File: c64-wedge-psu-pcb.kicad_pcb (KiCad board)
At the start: 2 copper layers, 70 x 54 mm, 22 parts, among them U1 LM2576T-ADJ

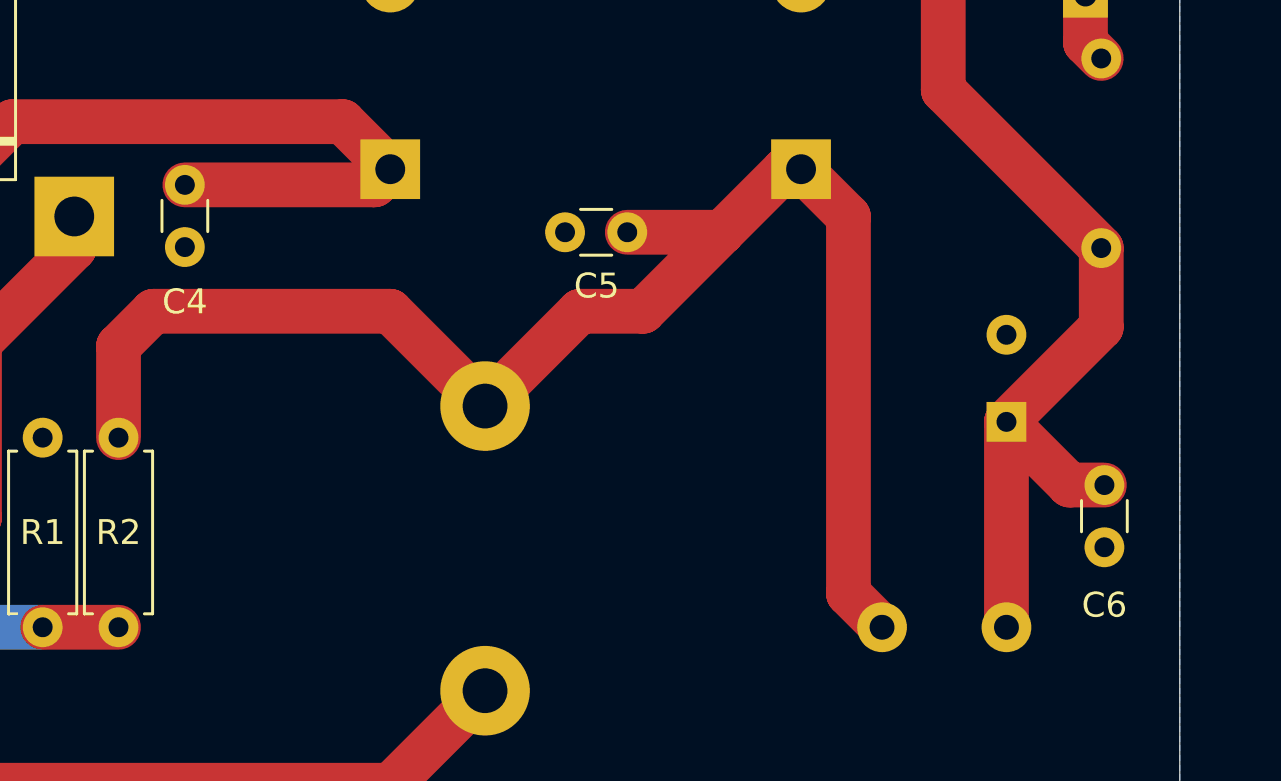
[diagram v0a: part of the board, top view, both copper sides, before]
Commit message: update ceramics with part number and update footprints
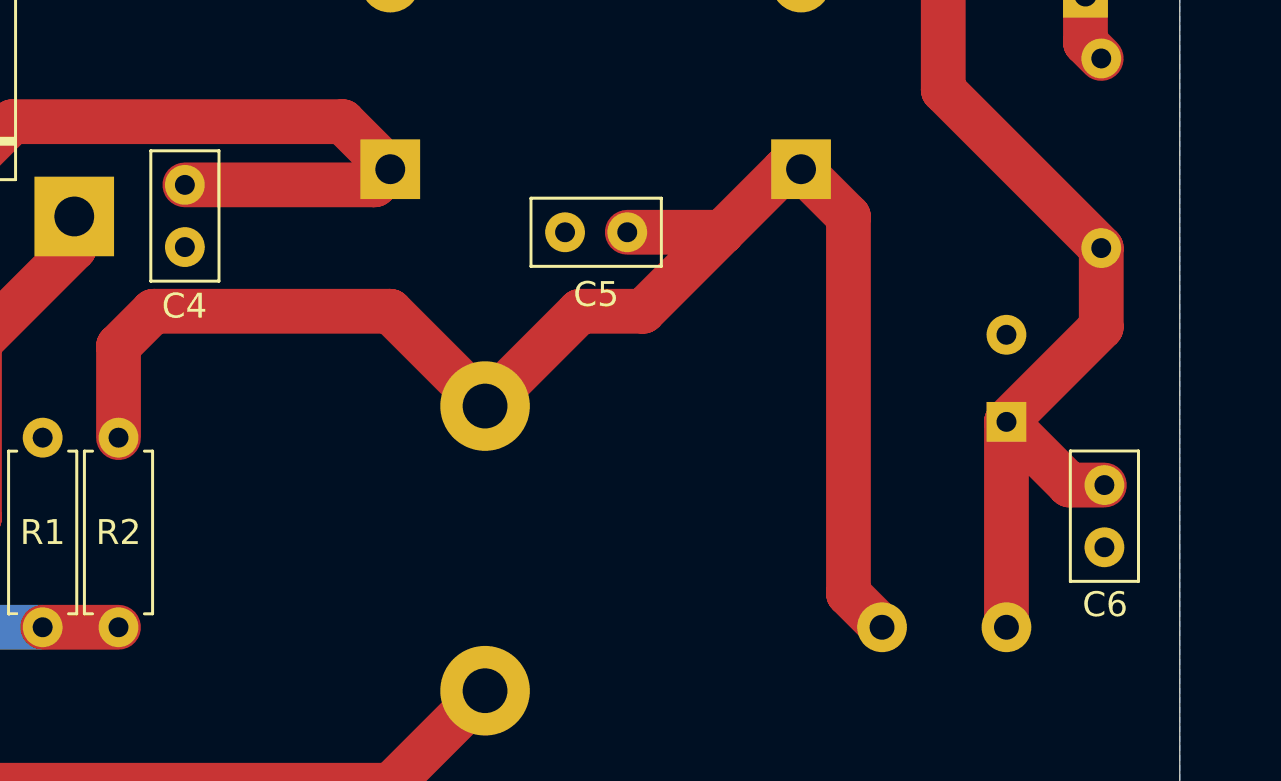
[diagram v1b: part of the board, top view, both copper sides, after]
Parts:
- C4, C5, C6: footprint Capacitor_THT:C_Disc_D3.0mm_W1.6mm_P2.50mm -> Capacitor_THT:C_Disc_D5.0mm_W2.5mm_P2.50mm

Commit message: updates
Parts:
- C1: footprint Capacitor_THT:CP_Radial_D16.0mm_P7.50mm -> Capacitor_THT:CP_Radial_D18.0mm_P7.50mm
- D1, D3, R1, R2: moved to B.Cu
- moved D5 19.9 mm to (107.2, 106.9), turned to 180 degrees
- moved C4 16.7 mm to (104.1, 92.7), turned to 180 degrees
- moved R2 15.5 mm to (110.2, 111.5), turned to 180 degrees
- moved R1 15.2 mm to (100.3, 111.5), turned to 180 degrees
- moved C3 5.22 mm to (157.0, 93.7), turned to 180 degrees
- moved L2 3.33 mm to (150.1, 102.1)
- moved C5 2.44 mm to (140.0, 90.7)
- moved R3 2.04 mm to (157.0, 88.1)
- moved LED1 1.93 mm to (157.0, 78.2)
- moved C2 1.42 mm to (146.1, 87.6)
- moved D4 1.27 mm to (94.0, 76.2)
- moved C6 1.09 mm to (158.0, 99.3)
- moved C1 0.68 mm to (128.5, 87.6)
- moved D1 0.64 mm to (111.1, 88.9)
- moved D3 0.64 mm to (99.7, 76.2)
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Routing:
- net Net-(C2-Pad1): track 60.8 -> 0.00 mm
- net Net-(D5-K): track 52.6 -> 0.11 mm
- net Net-(D1-K): track 45.3 -> 0.00 mm
- net /+5VDC: track 55.4 -> 49.4 mm
- net Net-(U1-FB): track 15.5 -> 12.4 mm
- net Net-(D2-A): track 28.9 -> 26.7 mm
- net Net-(D1-A): track 26.8 -> 27.9 mm
- net Net-(LED1-Pin_1): track 2.80 -> 2.29 mm
- added copper zone on F.Cu, net Net-(C2-Pad1)
- added copper zone on F.Cu, net Net-(D1-K)
- added copper zone on F.Cu, net Net-(D5-K)
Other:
- board text removed: "Output: 5V Max 3A"
- board text removed: "Ripple: <15mV"
- board text removed: "p-p"

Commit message: update
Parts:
- moved D5 9.91 mm to (117.1, 106.9)
- moved R1 1.30 mm to (101.6, 111.8)
- moved R2 1.30 mm to (111.5, 111.8)
- moved H3 0.65 mm to (142.0, 62.1)
- moved H2 0.65 mm to (112.0, 62.1)
- moved H1 0.65 mm to (104.0, 62.1)
- moved H4 0.65 mm to (150.0, 62.1)
- moved C6 0.51 mm to (157.5, 99.3)
- moved C4 0.51 mm to (104.6, 92.7)
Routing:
- net Net-(C2-Pad1): track 0.00 -> 43.6 mm
- net Net-(D2-A): track 26.7 -> 28.7 mm
- net Net-(D1-A): track 27.9 -> 28.5 mm

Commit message: Upgrade C1 to 5600uF and C2 to a better part, add some notes
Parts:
- C1: value 4700uF -> 5600uF
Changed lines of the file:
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@@
 		(sheetname "Root")
 		(sheetfile "c64-wedge-psu-pcb.kicad_sch")
-		(attr exclude_from_pos_files exclude_from_bom)
+		(attr exclude_from_pos_files)
 		(fp_line
 			(start -2.7 -2.45)
@@
 		(sheetname "Root")
 		(sheetfile "c64-wedge-psu-pcb.kicad_sch")
-		(attr exclude_from_pos_files exclude_from_bom)
+		(attr exclude_from_pos_files)
 		(fp_line
 			(start -2.7 -2.45)
@@
 		(sheetname "Root")
 		(sheetfile "c64-wedge-psu-pcb.kicad_sch")
-		(attr exclude_from_pos_files exclude_from_bom)
+		(attr exclude_from_pos_files)
 		(fp_line
 			(start -2.7 -2.45)
@@
 		(sheetname "Root")
 		(sheetfile "c64-wedge-psu-pcb.kicad_sch")
-		(attr exclude_from_pos_files exclude_from_bom)
+		(attr exclude_from_pos_files)
 		(fp_line
 			(start -2.7 -2.45)
@@
 			)
 		)
+		(property "Note" "1% Metal Film (1/4 W)"
+			(at 0 0 180)
+			(unlocked yes)
+			(layer "B.Fab")
+			(hide yes)
+			(effects
+				(font
+					(size 1 1)
+					(thickness 0.15)
+				)
+				(justify mirror)
+			)
+		)
 		(property ki_fp_filters "R_*")
 		(sheetname "Root")
@@
 			)
 		)
+		(property "Note" "1% Metal Film (1/4 W)"
+			(at 0 0 180)
+			(unlocked yes)
+			(layer "B.Fab")
+			(hide yes)
+			(effects
+				(font
+					(size 1 1)
+					(thickness 0.15)
+				)
+				(justify mirror)
+			)
+		)
 		(property ki_fp_filters "R_*")
 		(sheetname "Root")
@@
 			)
 		)
-		(property "Value" "4700uF"
+		(property "Value" "5600uF"
 			(at 3.75 -10.25 -90)
 			(layer "B.Fab")
@@
 			)
 		)
-		(property "Description" "UHW1E472MHD"
+		(property "Description" "UHW1E562MHD"
 			(at 0 0 -90)
 			(unlocked yes)
@@
 			)
 		)
+		(property "Note" "Footprint has 18mm diameter, even though the part is 16mm (to allow replacement for a bigger part)"
+			(at 0 0 90)
+			(unlocked yes)
+			(layer "B.Fab")
+			(hide yes)
+			(effects
+				(font
+					(size 1 1)
+					(thickness 0.15)
+				)
+				(justify mirror)
+			)
+		)
 		(property ki_fp_filters "CP_*")
 		(sheetname "Root")
@@
 			)
 		)
-		(property "Description" "UPW1E222MHD"
+		(property "Description" "UHW1E222MHD6"
 			(at 0 0 -90)
 			(unlocked yes)
@@
 			)
 		)
+		(property "Note" "1% Metal Film (1/4 W)"
+			(at 0 0 90)
+			(unlocked yes)
+			(layer "B.Fab")
+			(hide yes)
+			(effects
+				(font
+					(size 1 1)
+					(thickness 0.15)
+				)
+				(justify mirror)
+			)
+		)
 		(property ki_fp_filters "R_*")
 		(sheetname "Root")
@@
 		(tags "Diode DO-201AD series Axial Horizontal pin pitch 12.7mm  length 9.5mm diameter 5.2mm")
 		(property "Reference" "D5"
-			(at 6.35 0 360)
+			(at 6.35 0 0)
 			(layer "B.SilkS")
 			(effects
@@
 		)
 		(property "Value" "SB540"
-			(at 6.35 -3.72 360)
+			(at 6.35 -3.72 0)
 			(layer "B.Fab")
 			(effects
@@
 		)
 		(fp_text user "K"
-			(at 0 3.048 360)
+			(at 0 3.048 0)
 			(layer "B.SilkS")
 			(effects
@@
 		)
 		(fp_text user "K"
-			(at 0 2.6 360)
+			(at 0 2.6 0)
 			(layer "B.Fab")
 			(effects
@@
 		)
 		(fp_text user "${REFERENCE}"
-			(at 7.0625 0 360)
+			(at 7.0625 0 0)
 			(layer "B.Fab")
 			(effects

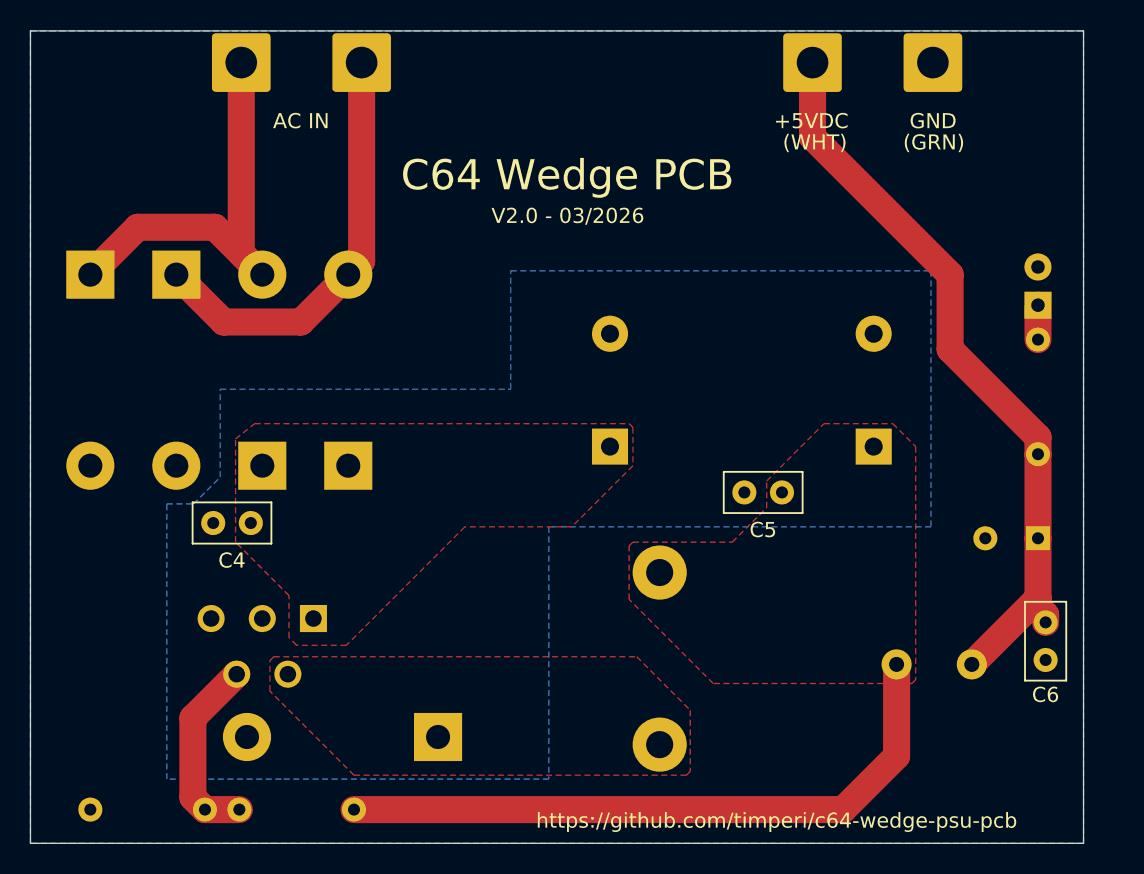
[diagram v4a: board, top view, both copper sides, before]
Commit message: PCB rev 2.0: docs, KiCad, gerbers, and release caveat
README clarifies U1 placement against the wedge inner (middle) wall, documents bench results and BOM notes, and states that V2.0 will be tagged only after the latest board is built, verified, and re-measured. Measurement checklist HTML is updated to match.

KiCad schematic/PCB/BOM refresh, wedge silk graphic footprint, wedge.gif, regenerated gerbers, and new gerber archive (replaces 2026-03-29 export).
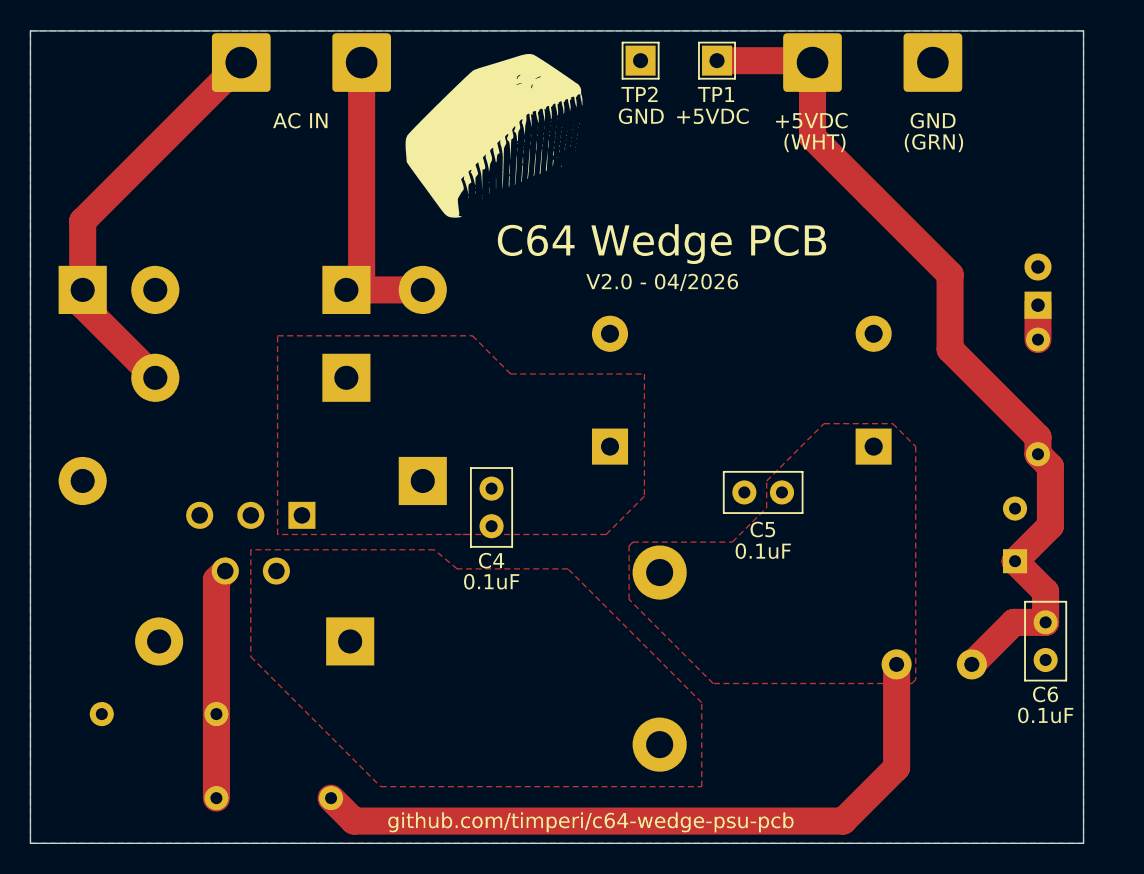
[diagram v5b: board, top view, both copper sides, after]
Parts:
- added G***: LOGO, c64-wedge-psu-pcb:wedge-image, F.Cu at (121.0, 67.0)
- added TP1: +5VDC, TestPoint:TestPoint_THTPad_2.0x2.0mm_Drill1.0mm, F.Cu at (135.6, 62.0)
- added TP2: GND, TestPoint:TestPoint_THTPad_2.0x2.0mm_Drill1.0mm, F.Cu at (130.6, 62.0)
- R2: value 3.2k -> 3.3k
- R3: value 200 -> 220
- moved C4 16.2 mm to (120.7, 90.4), turned to -90 degrees
- moved D3 11.3 mm to (111.0, 77.2), turned to 180 degrees
- moved D5 8.63 mm to (111.3, 100.6)
- moved D2 8.08 mm to (111.0, 83.1), turned to 180 degrees
- moved U1 6.90 mm to (108.0, 92.2)
- moved R1 6.40 mm to (102.4, 105.4)
- moved D1 5.06 mm to (116.1, 89.9)
- moved C3 2.16 mm to (155.4, 95.2), turned to 90 degrees
- moved R2 1.70 mm to (110.0, 111.0)
- moved D4 1.14 mm to (93.5, 77.2)
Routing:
- net /+5VDC: track 49.8 -> 58.0 mm
- net Net-(D1-A): track 28.5 -> 20.6 mm
- net Net-(C2-Pad1): track 43.6 -> 46.6 mm
- net Net-(U1-FB): track 12.8 -> 15.3 mm
- net Net-(D2-A): track 28.7 -> 27.3 mm
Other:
- board text added: "- Short leg"
- board text added: "ADD HEATSINK!"
- board text added: "V2.0 - 04/2026"
- board text added: "github.com/timperi/c64-wedge-psu-pcb"
- board text removed: "V2.0 - 03/2026"
- board text removed: "https://github.com/timperi/c64-wedge-psu-pcb"

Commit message: PCB layout refresh, gerbers, measurements tree, UBEC memo
KiCad schematic/PCB/project updates; regenerated gerbers and gerber zip (2026-04-12).

Add measurements/ index with LM2576-rev2-e-load write-up, UBEC-2026-04-11 captures + README, historical-100us placeholder. README points to measurement pages.

Add printable UBEC vs PCB comparison memo (docs). Remove old gerber-2026-04-11.zip.
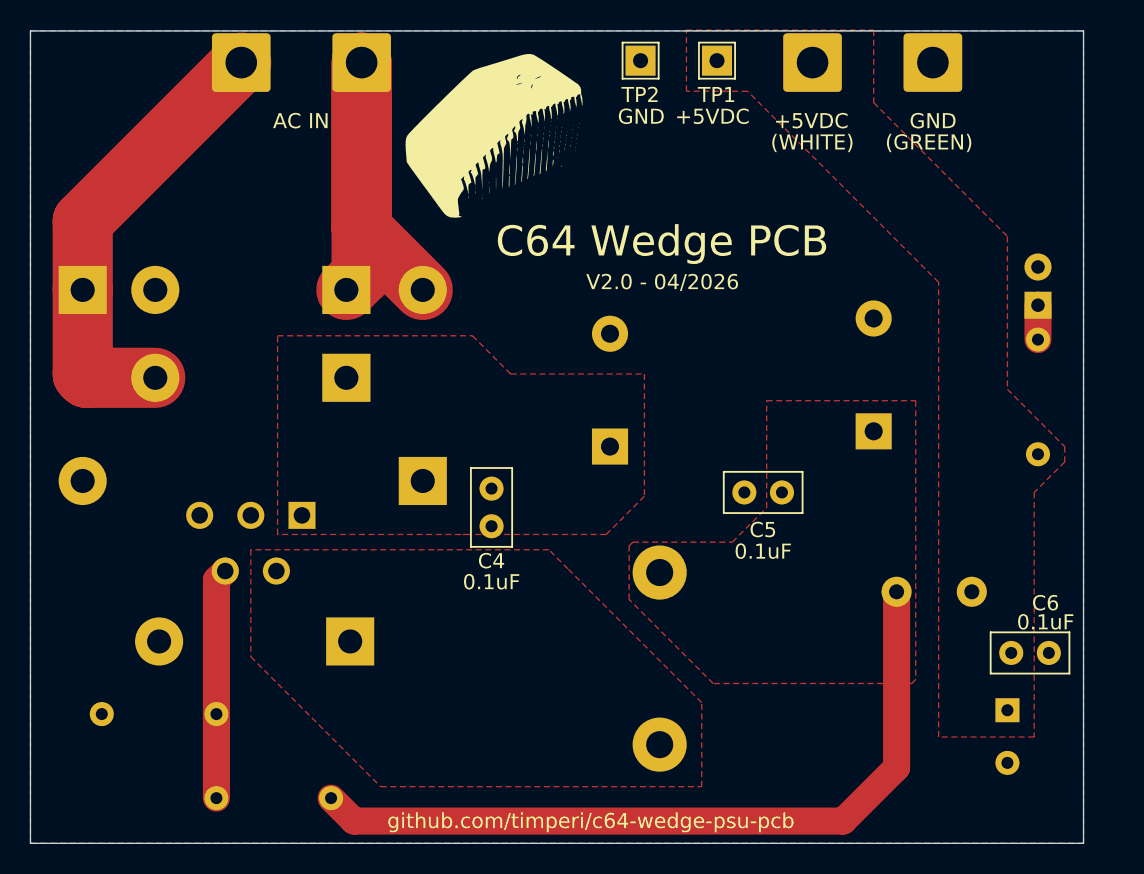
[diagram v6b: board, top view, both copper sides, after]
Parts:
- moved C3 9.92 mm to (154.9, 105.2), turned to -90 degrees
- moved L2 4.83 mm to (150.1, 97.3)
- moved C6 3.06 mm to (155.2, 101.3), turned to 0 degrees
- moved C2 1.02 mm to (146.1, 86.6)
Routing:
- net /+5VDC: track 58.0 -> 0.18 mm
- net Net-(D1-A): track 20.6 -> 32.3 mm
- net Net-(C2-Pad1): track 46.6 -> 51.4 mm
- net Net-(D2-A): track 27.3 -> 30.0 mm
- added copper zone on F.Cu, net /+5VDC
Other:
- board text added: "(GREEN)"
- board text added: "(WHITE)"
- board text removed: "(GRN)"
- board text removed: "(WHT)"
